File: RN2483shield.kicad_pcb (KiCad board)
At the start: 2 copper layers, 57.9 x 53.6 mm, 27 parts, among them J1 LoRa_GPIO, J2 SMA_HF, Q1 BSS138, Q2 BSS138, U1 RN2483/RN2903

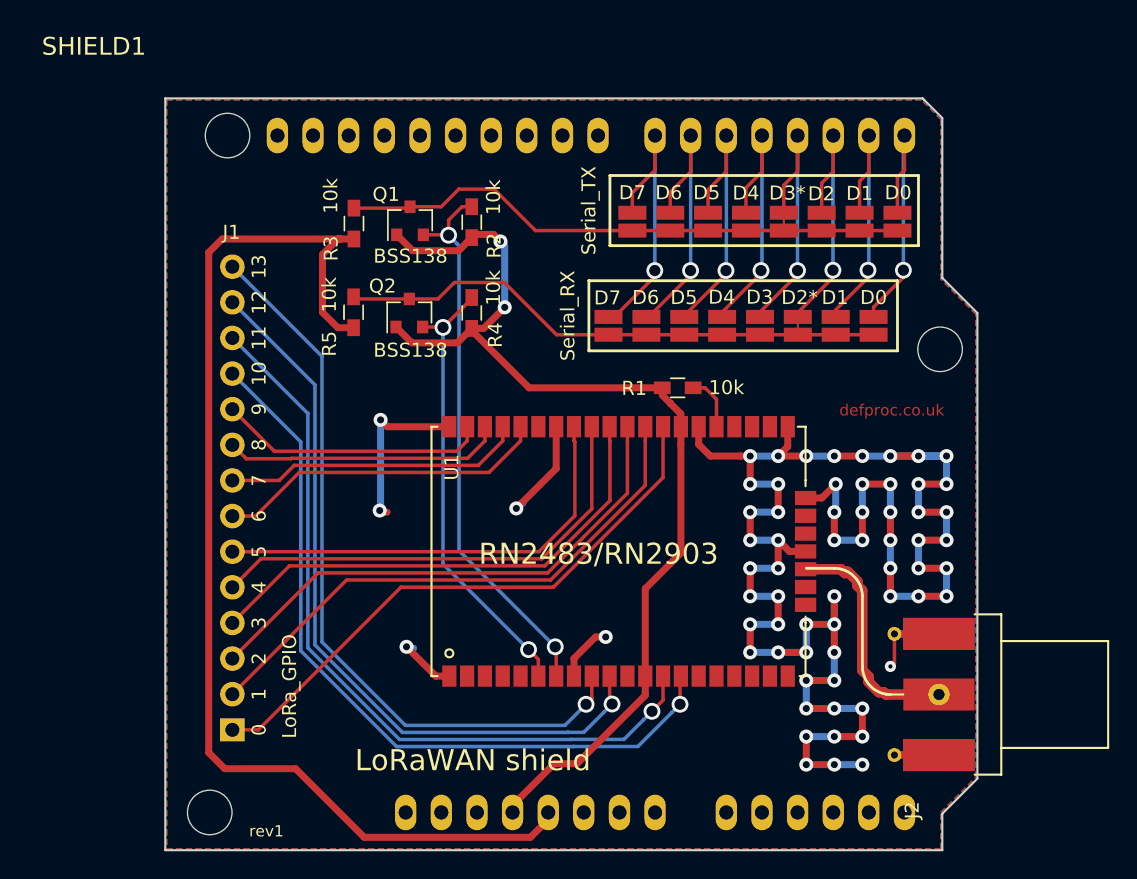
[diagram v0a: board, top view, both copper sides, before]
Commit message: EOD: redrafted board with new level shifters
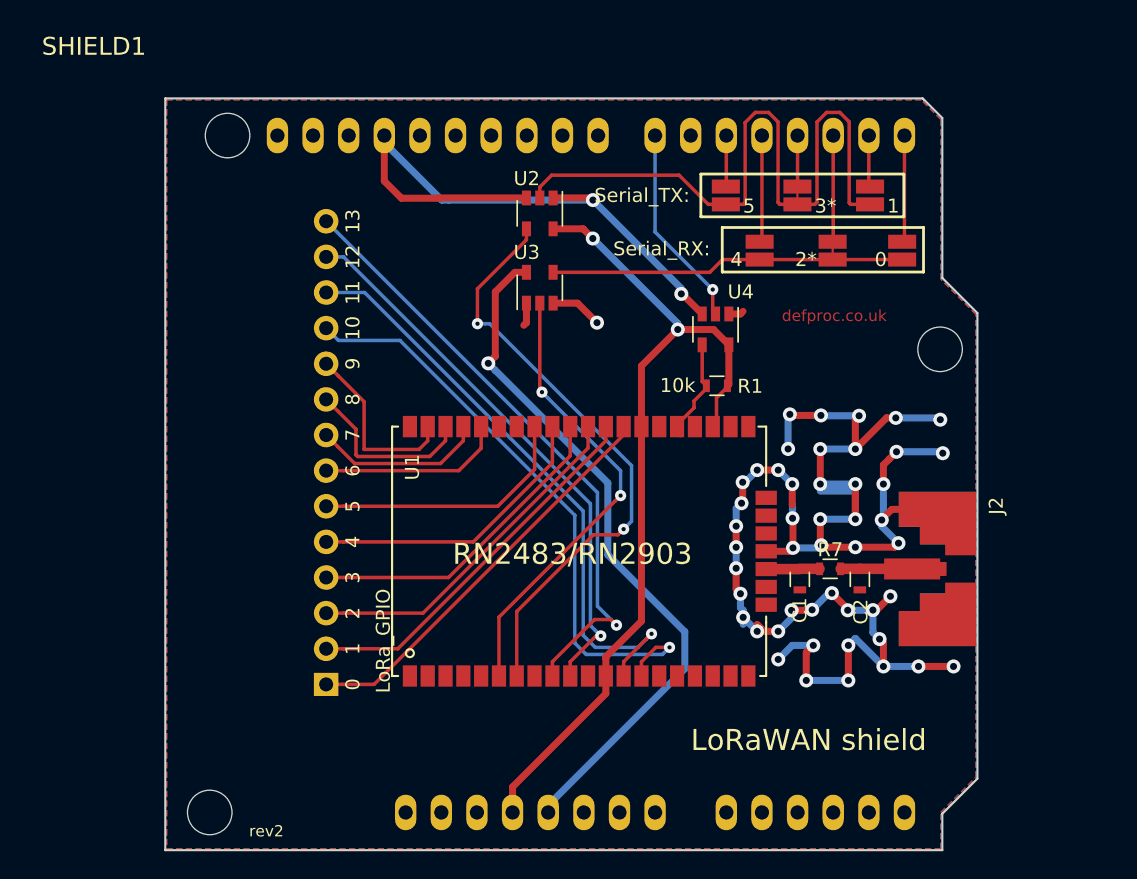
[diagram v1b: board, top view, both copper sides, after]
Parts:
- removed D0 (x2), D1 (x2), D2, D3, D4 (x2), D5 (x2), D6 (x2), D7 (x2): Jumper_NO_Small, MyFootprints:NO_SMD_JPR
- removed D2*, D3*: Jumper_NC_Small, MyFootprints:NC_SMD_JPR
- removed Q1, Q2: BSS138, TO_SOT_Packages_SMD:SOT-23
- removed R2, R3, R4, R5: 10k, Resistors_SMD:R_0603_HandSoldering
- added C1: NC, Resistors_SMD:R_0603, F.Cu at (204.5, 85.8)
- added C2: NC, Resistors_SMD:R_0603, F.Cu at (208.8, 85.8)
- added JP1: Jumper_NO_Small, MyFootprints:NO_SMD_JPR, F.Cu at (211.8, 63.0)
- added JP2: Jumper_NO_Small, MyFootprints:NO_SMD_JPR, F.Cu at (209.6, 59.1)
- added JP3: Jumper_NC_Small, MyFootprints:NC_SMD_JPR, F.Cu at (206.9, 63.0)
- added JP4: Jumper_NC_Small, MyFootprints:NC_SMD_JPR, F.Cu at (204.4, 59.1)
- added JP5: Jumper_NO_Small, MyFootprints:NO_SMD_JPR, F.Cu at (201.7, 63.0)
- added JP6: Jumper_NO_Small, MyFootprints:NO_SMD_JPR, F.Cu at (199.3, 59.1)
- added R7: 0R, Resistors_SMD:R_0603, F.Cu at (206.7, 85.0)
- added U2: SN74LVC1G125, TO_SOT_Packages_SMD:SOT-23-5, F.Cu at (186.0, 59.7)
- added U3: SN74LVC1G125, TO_SOT_Packages_SMD:SOT-23-5, F.Cu at (186.0, 65.0)
- added U4: SN74LVC1G125, TO_SOT_Packages_SMD:SOT-23-5, F.Cu at (198.5, 68.0)
- J2: footprint MyFootprints:SMA_Edge -> MyFootprints:multi-rf-sma-ufl
- R1: footprint Resistors_SMD:R_0603_HandSoldering -> Resistors_SMD:R_0603
- moved J2 8.95 mm to (217.1, 85.0)
- moved J1 7.43 mm to (170.8, 76.8)
- moved U1 2.81 mm to (175.5, 74.9)
- moved R1 2.80 mm to (198.6, 72.0), turned to 0 degrees
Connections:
- J2 pad 1: Net-(J2-Pad1) -> Net-(C2-Pad1)
- SHIELD1 pad 6: D6 -> (no net)
- U1 pad 23: Net-(J2-Pad1) -> Net-(C1-Pad1)
- U1 pad 25: Net-(J3-Pad1) -> (no net)
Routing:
- net Net-(JP2-Pad1): track 0.00 -> 49.7 mm
- net Net-(JP10-Pad1): track 39.3 -> 0.00 mm
- net +5V: track 82.7 -> 50.0 mm, vias 0 -> 1
- net D6: track 20.4 -> 0.00 mm, vias 1 -> 0
- net GND: track 162.9 -> 181.4 mm, vias 64 -> 51
- net Net-(J2-Pad1): track 17.0 -> 0.00 mm
- net D5: track 20.2 -> 3.65 mm, vias 1 -> 0
- net D3_TX: track 20.0 -> 3.64 mm, vias 1 -> 0
- net D1: track 19.7 -> 3.67 mm, vias 1 -> 0
- net Net-(JP1-Pad1): track 40.7 -> 25.3 mm
- net GPIO_12: track 53.5 -> 39.8 mm
- net GPIO_4: track 34.2 -> 21.0 mm
- net GPIO_5: track 31.8 -> 19.0 mm
- net GPIO_3: track 35.8 -> 23.1 mm
- net GPIO_2: track 37.8 -> 25.1 mm
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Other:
- board text added: "0"
- board text added: "1"
- board text added: "2*"
- board text added: "3*"
- board text added: "4"
- board text added: "5"
- board text added: "Serial_RX:"
- board text added: "Serial_TX:"
- board text added: "rev2"
- board text removed: "Serial_RX"
- board text removed: "Serial_TX"
- board text removed: "rev1"
